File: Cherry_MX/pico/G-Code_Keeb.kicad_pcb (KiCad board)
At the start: 2 copper layers, 158.7 x 133.3 mm, 28 parts, among them SW1 SW_Push_45deg, SW10 SW_Push_45deg, SW11 SW_Push_45deg, SW12 SW_Push_45deg, SW13 SW_Push_45deg, SW14 SW_Push_45deg, SW15 SW_Push_45deg, SW16 SW_Push_45deg, SW17 SW_Push_45deg, SW18 SW_Push_45deg, SW19 SW_Push_45deg, SW2 SW_Push_45deg, SW20 SW_Push_45deg, SW21 SW_Push_45deg, SW22 SW_Push_45deg, SW23 SW_Push_45deg, SW3 SW_Push_45deg, SW4 SW_Push_45deg, SW5 SW_Push_45deg, SW6 SW_Push_45deg, SW7 SW_Push_45deg, SW8 SW_Push_45deg, SW9 SW_Push_45deg, U1 Pico

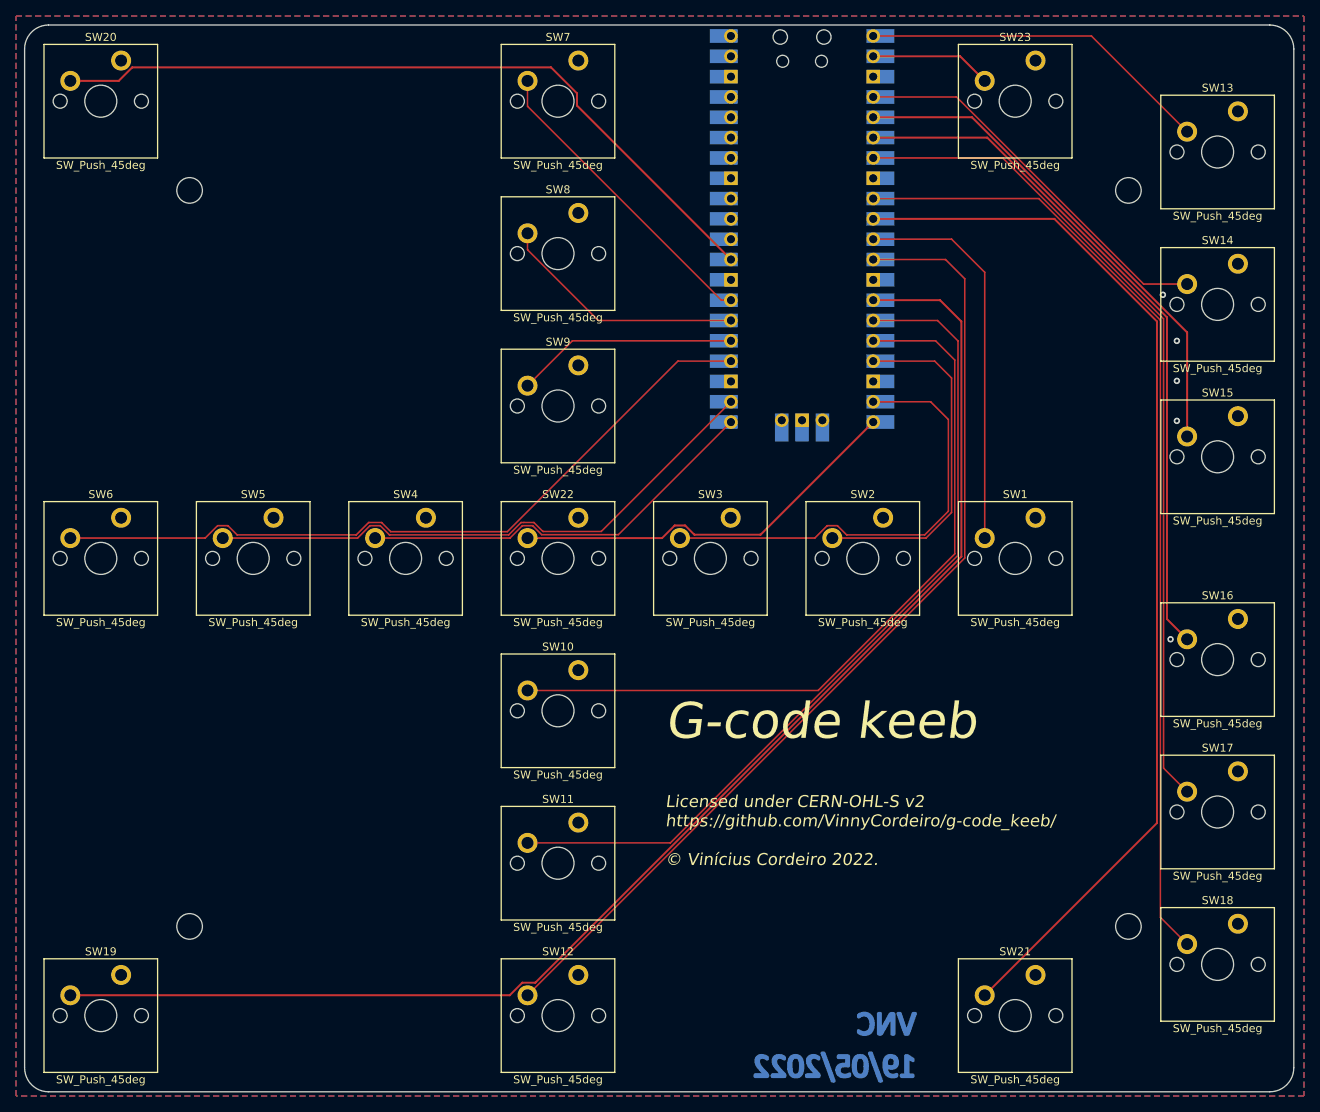
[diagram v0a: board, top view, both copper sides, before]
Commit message: Updating silkscreen
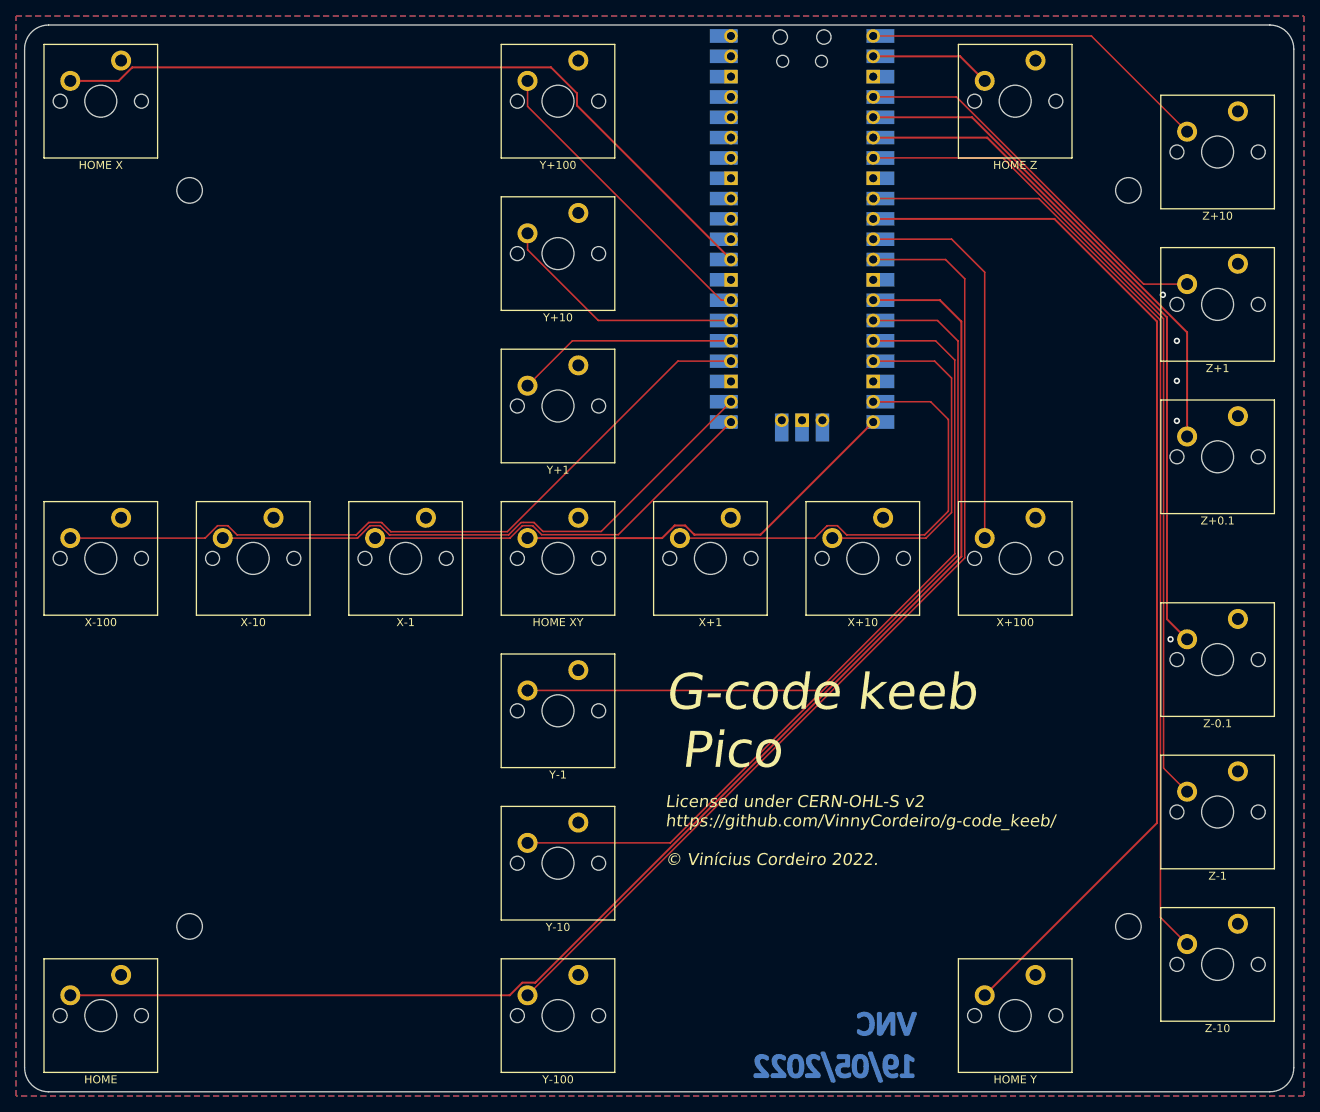
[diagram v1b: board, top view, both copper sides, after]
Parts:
- SW1: value SW_Push_45deg -> X+100
- SW10: value SW_Push_45deg -> Y-1
- SW11: value SW_Push_45deg -> Y-10
- SW12: value SW_Push_45deg -> Y-100
- SW13: value SW_Push_45deg -> Z+10
- SW14: value SW_Push_45deg -> Z+1
- SW15: value SW_Push_45deg -> Z+0.1
- SW16: value SW_Push_45deg -> Z-0.1
- SW17: value SW_Push_45deg -> Z-1
- SW18: value SW_Push_45deg -> Z-10
- SW19: value SW_Push_45deg -> HOME
- SW2: value SW_Push_45deg -> X+10
- SW20: value SW_Push_45deg -> HOME X
- SW21: value SW_Push_45deg -> HOME Y
- SW22: value SW_Push_45deg -> HOME XY
- SW23: value SW_Push_45deg -> HOME Z
- SW3: value SW_Push_45deg -> X+1
- SW4: value SW_Push_45deg -> X-1
- SW4: renamed from SW6; value SW_Push_45deg -> X-100
- SW5: value SW_Push_45deg -> X-10
- SW7: value SW_Push_45deg -> Y+100
- SW8: value SW_Push_45deg -> Y+10
- SW9: value SW_Push_45deg -> Y+1
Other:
- board text added: "G-code keeb Pico"
- board text removed: "G-code keeb"
